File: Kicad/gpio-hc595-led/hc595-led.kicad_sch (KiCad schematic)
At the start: 8 parts, among them K1 GPIO IN, K2 GPIO OUT, K3 DATA OUT, U1 74HC595, U2 3M-SJ5376

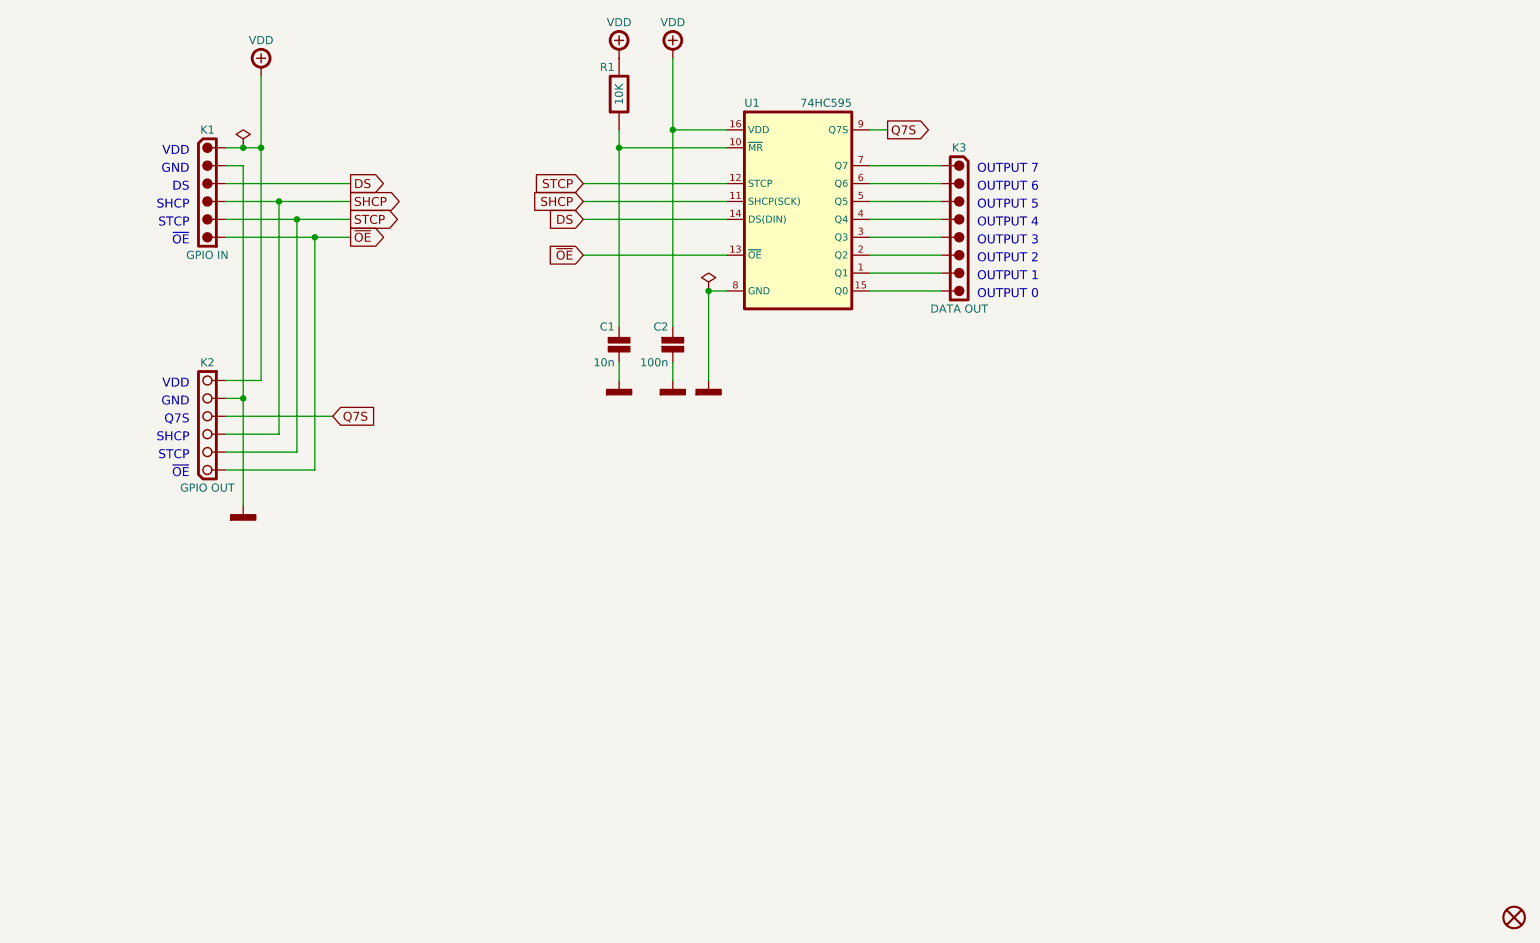
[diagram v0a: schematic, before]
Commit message: GPIO HC595
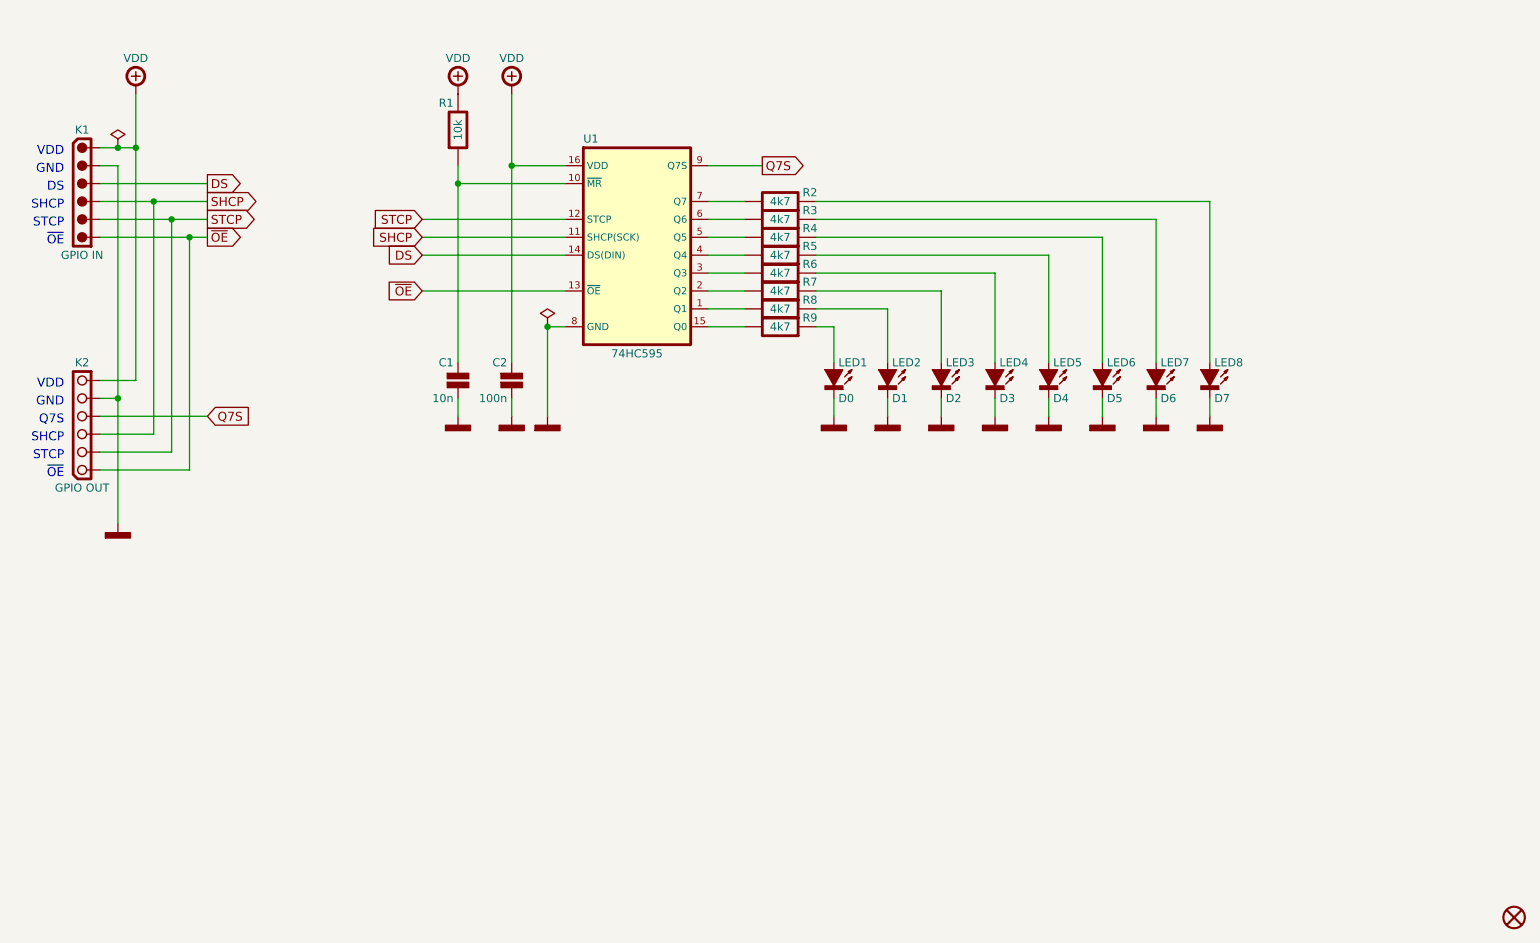
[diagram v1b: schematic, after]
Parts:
- removed K3: DATA OUT, tronixio:HARWIN-M20-999084x, symbol tronixio:HARWIN-254-M-1X08-VERTICAL
- added LED1: D0, tronixio:LED-SMD-1206, symbol tronixio:KINGBRIGHT-LED-1206-RED
- added LED2: D1, tronixio:LED-SMD-1206, symbol tronixio:KINGBRIGHT-LED-1206-RED
- added LED3: D2, tronixio:LED-SMD-1206, symbol tronixio:KINGBRIGHT-LED-1206-RED
- added LED4: D3, tronixio:LED-SMD-1206, symbol tronixio:KINGBRIGHT-LED-1206-RED
- added LED5: D4, tronixio:LED-SMD-1206, symbol tronixio:KINGBRIGHT-LED-1206-RED
- added LED6: D5, tronixio:LED-SMD-1206, symbol tronixio:KINGBRIGHT-LED-1206-RED
- added LED7: D6, tronixio:LED-SMD-1206, symbol tronixio:KINGBRIGHT-LED-1206-RED
- added LED8: D7, tronixio:LED-SMD-1206, symbol tronixio:KINGBRIGHT-LED-1206-RED
- added R2, R3, R4, R5, R6, R7, R8, R9: 4k7, tronixio:RESISTOR-SMD-1206, symbol tronixio:RESISTOR-1206-4K7-5P
- R1: value 10K -> 10k
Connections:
- net at U1.7 (Q7): now also R2.1
- net at U1.6 (Q6): now also R3.1
- net at U1.5 (Q5): now also R4.1
- net at U1.4 (Q4): now also R5.1
- net at U1.3 (Q3): now also R6.1
- net at U1.2 (Q2): now also R7.1
- net at U1.1 (Q1): now also R8.1
- net at U1.15 (Q0): now also R9.1
- net POWER-GND renamed GND
- net GND: now also LED1.1 (C), LED2.1 (C), LED3.1 (C), LED4.1 (C), LED5.1 (C), LED6.1 (C), LED7.1 (C), LED8.1 (C)
- net POWER-VBAT renamed +VDD
- new net: LED7.2 (A), R3.2
- new net: LED5.2 (A), R5.2
- new net: LED8.2 (A), R2.2
- new net: LED2.2 (A), R8.2
- new net: LED4.2 (A), R6.2
- new net: LED1.2 (A), R9.2
- new net: LED3.2 (A), R7.2
- new net: LED6.2 (A), R4.2
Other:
- note removed: "OUTPUT 0"
- note removed: "OUTPUT 1"
- note removed: "OUTPUT 2"
- note removed: "OUTPUT 3"
- note removed: "OUTPUT 4"
- note removed: "OUTPUT 5"
- note removed: "OUTPUT 6"
- note removed: "OUTPUT 7"
- title: GPIO - 74HC595-HEADER -> GPIO - 74HC595-LED
- moved on the sheet: K1, K2, U1
